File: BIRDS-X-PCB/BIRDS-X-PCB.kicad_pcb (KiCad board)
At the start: 2 copper layers, 85 x 85 mm, 0 parts

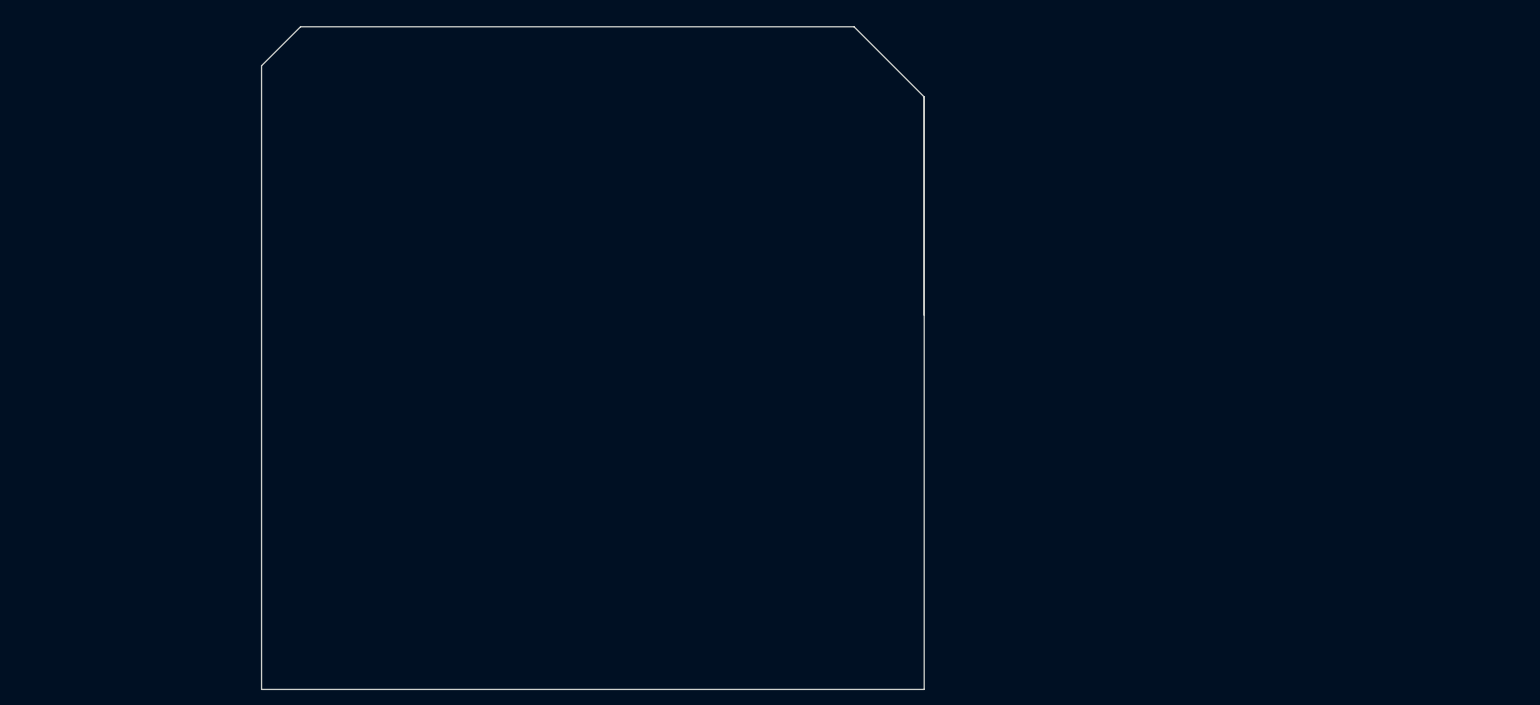
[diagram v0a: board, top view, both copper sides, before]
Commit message: Add core restricted layouts and lock them
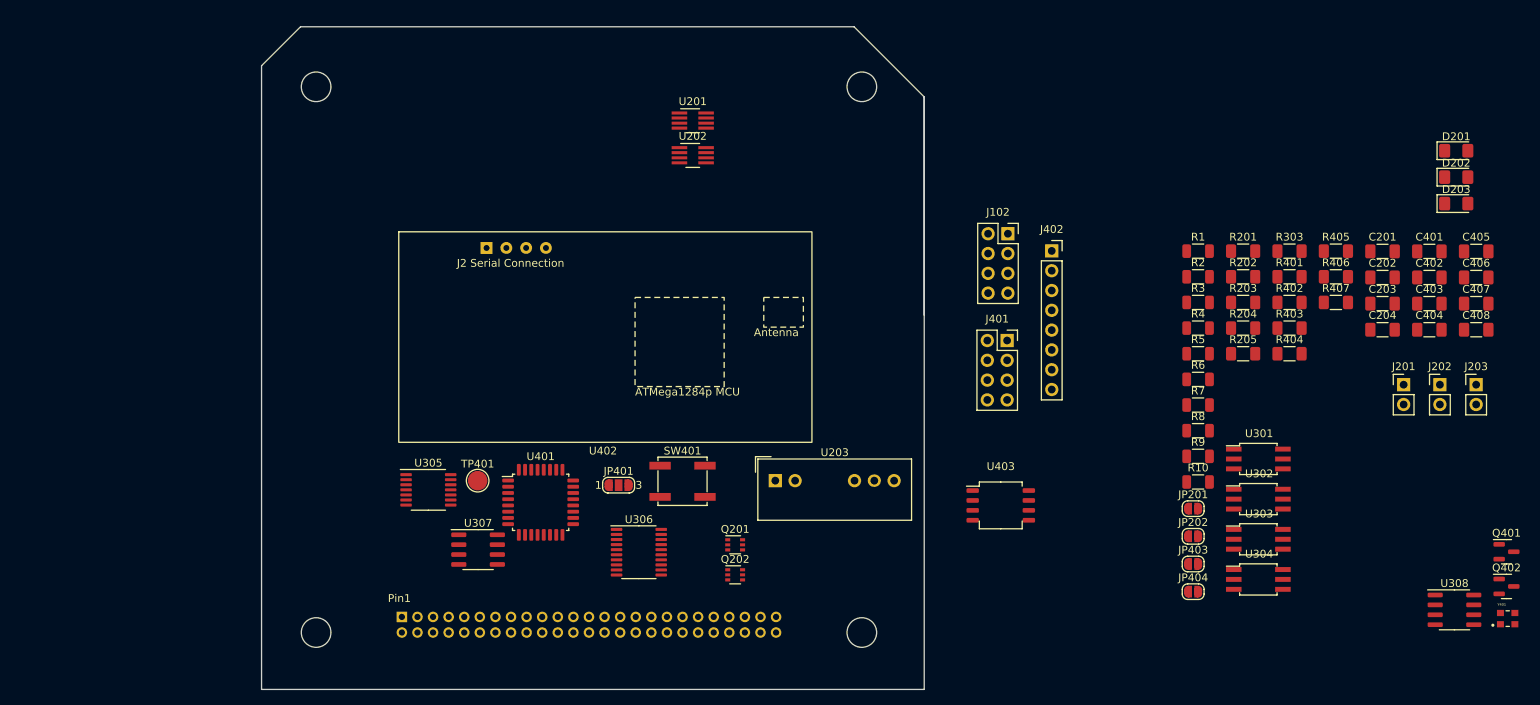
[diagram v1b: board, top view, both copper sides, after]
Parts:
- added C201: 10u, Capacitor_SMD:C_1206_3216Metric_Pad1.33x1.80mm_HandSolder, F.Cu at (225.3, 79.8)
- added C202: 10u, Capacitor_SMD:C_1206_3216Metric_Pad1.33x1.80mm_HandSolder, F.Cu at (225.3, 83.2)
- added C203: 4.7u, Capacitor_SMD:C_1206_3216Metric_Pad1.33x1.80mm_HandSolder, F.Cu at (225.3, 86.5)
- added C204: 10u, Capacitor_SMD:C_1206_3216Metric_Pad1.33x1.80mm_HandSolder, F.Cu at (225.3, 89.9)
- added C401: 100n, Capacitor_SMD:C_1206_3216Metric_Pad1.33x1.80mm_HandSolder, F.Cu at (231.3, 79.8)
- added C402: 100n, Capacitor_SMD:C_1206_3216Metric_Pad1.33x1.80mm_HandSolder, F.Cu at (231.3, 83.2)
- added C403: 4.7u, Capacitor_SMD:C_1206_3216Metric_Pad1.33x1.80mm_HandSolder, F.Cu at (231.3, 86.5)
- added C404: 10n, Capacitor_SMD:C_1206_3216Metric_Pad1.33x1.80mm_HandSolder, F.Cu at (231.3, 89.9)
- added C405: 100n, Capacitor_SMD:C_1206_3216Metric_Pad1.33x1.80mm_HandSolder, F.Cu at (237.3, 79.8)
- added C406: 4.7u, Capacitor_SMD:C_1206_3216Metric_Pad1.33x1.80mm_HandSolder, F.Cu at (237.3, 83.2)
- added C407: 100n, Capacitor_SMD:C_1206_3216Metric_Pad1.33x1.80mm_HandSolder, F.Cu at (237.3, 86.5)
- added C408: 4.7u, Capacitor_SMD:C_1206_3216Metric_Pad1.33x1.80mm_HandSolder, F.Cu at (237.3, 89.9)
- added D201: LED, LED_SMD:LED_1206_3216Metric_Pad1.42x1.75mm_HandSolder, F.Cu at (234.7, 66.9)
- added D202: LED, LED_SMD:LED_1206_3216Metric_Pad1.42x1.75mm_HandSolder, F.Cu at (234.7, 70.3)
- added D203: LED, LED_SMD:LED_1206_3216Metric_Pad1.42x1.75mm_HandSolder, F.Cu at (234.7, 73.7)
- added H101: MountingHole, BIRDS-X_Footprints_Lib:MountingHole_3.8mm, F.Cu at (88.5, 58.7)
- added H102: MountingHole, BIRDS-X_Footprints_Lib:MountingHole_3.8mm, F.Cu at (158.5, 58.7)
- added H103: MountingHole, BIRDS-X_Footprints_Lib:MountingHole_3.8mm, F.Cu at (88.5, 128.7)
- added H104: MountingHole, BIRDS-X_Footprints_Lib:MountingHole_3.8mm, F.Cu at (158.5, 128.7)
- added J101: LPC-50M2LG, Connector_PinHeader_2.00mm:PinHeader_2x25_P2.00mm_Horizontal, B.Cu at (99.5, 126.7)
- added J102: Conn_02x04_Odd_Even, Connector_PinSocket_2.54mm:PinSocket_2x04_P2.54mm_Vertical, F.Cu at (177.2, 77.5)
- added J201: Conn_01x02, Connector_PinHeader_2.54mm:PinHeader_1x02_P2.54mm_Vertical, F.Cu at (228.0, 96.9)
- added J202: Conn_01x02, Connector_PinHeader_2.54mm:PinHeader_1x02_P2.54mm_Vertical, F.Cu at (232.7, 96.9)
- added J203: Conn_01x02, Connector_PinHeader_2.54mm:PinHeader_1x02_P2.54mm_Vertical, F.Cu at (237.3, 96.9)
- added J401: Conn_02x04_Odd_Even, Connector_PinSocket_2.54mm:PinSocket_2x04_P2.54mm_Vertical, F.Cu at (177.1, 91.2)
- added J402: Conn_01x08, Connector_PinSocket_2.54mm:PinSocket_1x08_P2.54mm_Vertical, F.Cu at (182.9, 79.8)
- added JP201: Jumper_2_Open, Jumper:SolderJumper-2_P1.3mm_Open_RoundedPad1.0x1.5mm, F.Cu at (201.0, 112.8)
- added JP202: Jumper_2_Open, Jumper:SolderJumper-2_P1.3mm_Open_RoundedPad1.0x1.5mm, F.Cu at (201.0, 116.4)
- added JP401: Jumper_3_Open, Jumper:SolderJumper-3_P1.3mm_Open_RoundedPad1.0x1.5mm_NumberLabels, F.Cu at (127.3, 109.8)
- added JP403: Jumper_2_Open, Jumper:SolderJumper-2_P1.3mm_Open_RoundedPad1.0x1.5mm, F.Cu at (201.0, 119.9)
- added JP404: Jumper_2_Open, Jumper:SolderJumper-2_P1.3mm_Open_RoundedPad1.0x1.5mm, F.Cu at (201.0, 123.5)
- added Q201: SI1470DH, Package_TO_SOT_SMD:SOT-363_SC-70-6, F.Cu at (142.2, 117.5)
- added Q202: SI1470DH, Package_TO_SOT_SMD:SOT-363_SC-70-6, F.Cu at (142.2, 121.3)
- added Q401: BSS138, Package_TO_SOT_SMD:SOT-23, F.Cu at (241.2, 118.3)
- added Q402: BSS138, Package_TO_SOT_SMD:SOT-23, F.Cu at (241.2, 122.8)
- added R1: 390k, Resistor_SMD:R_1206_3216Metric, F.Cu at (201.6, 79.8)
- added R10: 3.6M, Resistor_SMD:R_1206_3216Metric, F.Cu at (201.6, 109.4)
- added R2: 10k, Resistor_SMD:R_1206_3216Metric, F.Cu at (201.6, 83.1)
- added R201: 0.025, PE1206FRE470R025L, Resistor_SMD:R_1206_3216Metric_Pad1.30x1.75mm_HandSolder, F.Cu at (207.4, 79.8)
- added R202: 0.025, PE1206FRE470R025L, Resistor_SMD:R_1206_3216Metric_Pad1.30x1.75mm_HandSolder, F.Cu at (207.4, 83.1)
- added R203: R, Resistor_SMD:R_1206_3216Metric_Pad1.30x1.75mm_HandSolder, F.Cu at (207.4, 86.4)
- added R204: R, Resistor_SMD:R_1206_3216Metric_Pad1.30x1.75mm_HandSolder, F.Cu at (207.4, 89.7)
- added R205: R, Resistor_SMD:R_1206_3216Metric_Pad1.30x1.75mm_HandSolder, F.Cu at (207.4, 92.9)
- added R3: 10M, Resistor_SMD:R_1206_3216Metric, F.Cu at (201.6, 86.4)
- added R303: 3.3k, Resistor_SMD:R_1206_3216Metric_Pad1.30x1.75mm_HandSolder, F.Cu at (213.4, 79.8)
- added R4: 3.6M, Resistor_SMD:R_1206_3216Metric, F.Cu at (201.6, 89.7)
- added R401: 3.3k, Resistor_SMD:R_1206_3216Metric_Pad1.30x1.75mm_HandSolder, F.Cu at (213.4, 83.1)
- added R402: 3.3k, Resistor_SMD:R_1206_3216Metric_Pad1.30x1.75mm_HandSolder, F.Cu at (213.4, 86.4)
- added R403: 10k, Resistor_SMD:R_1206_3216Metric_Pad1.30x1.75mm_HandSolder, F.Cu at (213.4, 89.7)
- added R404: 10k, Resistor_SMD:R_1206_3216Metric_Pad1.30x1.75mm_HandSolder, F.Cu at (213.4, 92.9)
- added R405: 10k, Resistor_SMD:R_1206_3216Metric_Pad1.30x1.75mm_HandSolder, F.Cu at (219.3, 79.8)
- added R406: 10k, Resistor_SMD:R_1206_3216Metric_Pad1.30x1.75mm_HandSolder, F.Cu at (219.3, 83.1)
- added R407: 10k, Resistor_SMD:R_1206_3216Metric_Pad1.30x1.75mm_HandSolder, F.Cu at (219.3, 86.4)
- added R5: 10M, Resistor_SMD:R_1206_3216Metric, F.Cu at (201.6, 92.9)
- added R6: 3.6M, Resistor_SMD:R_1206_3216Metric, F.Cu at (201.6, 96.2)
- added R7: 10M, Resistor_SMD:R_1206_3216Metric, F.Cu at (201.6, 99.5)
- added R8: 3.6M, Resistor_SMD:R_1206_3216Metric, F.Cu at (201.6, 102.8)
- added R9: 10M, Resistor_SMD:R_1206_3216Metric, F.Cu at (201.6, 106.1)
- added SW401: SW_Push, Button_Switch_SMD:SW_SPST_EVPBF, F.Cu at (135.5, 109.3)
- added TP401: TestPoint, TestPoint:TestPoint_Pad_D2.5mm, F.Cu at (109.2, 109.2)
- added U201: LTC4361-X, Package_TO_SOT_SMD:TSOT-23-8_HandSoldering, F.Cu at (136.8, 63.0)
- added U202: LTC4361-X, Package_TO_SOT_SMD:TSOT-23-8_HandSoldering, F.Cu at (136.8, 67.5)
- added U203: 0.1S7B_3UP, BIRDS-X_Footprints_Lib:Converter_DCDC_Gaptec_0.1S7B_3UP_THT, F.Cu at (147.4, 109.2)
- added U301: VT01, Package_SO:SO-6_4.4x3.6mm_P1.27mm, F.Cu at (209.4, 106.4)
- added U302: VT01, Package_SO:SO-6_4.4x3.6mm_P1.27mm, F.Cu at (209.4, 111.6)
- added U303: VT01, Package_SO:SO-6_4.4x3.6mm_P1.27mm, F.Cu at (209.4, 116.7)
- added U304: VT01, Package_SO:SO-6_4.4x3.6mm_P1.27mm, F.Cu at (209.4, 121.9)
- added U305: TL974IPWR, Package_SO:TSSOP-14_4.4x5mm_P0.65mm, F.Cu at (102.9, 110.4)
- added U306: ADG734, Package_SO:TSSOP-20_4.4x6.5mm_P0.65mm, F.Cu at (129.9, 118.4)
- added U307: LM335DT, Package_SO:SOIC-8_3.9x4.9mm_P1.27mm, F.Cu at (109.3, 118.1)
- added U308: LM334M, Package_SO:SOIC-8_3.9x4.9mm_P1.27mm, F.Cu at (234.5, 125.8)
- added U401: STM32G031K8Tx, Package_QFP:LQFP-32_7x7mm_P0.8mm, F.Cu at (117.3, 112.0)
- added U402: MTT4B-Mini, BIRDS-X_Footprints_Lib:MTT4B-Mini, F.Cu at (125.6, 90.8)
- added U403: MT29F2G01ABAGDWB-IT-G_TR, BIRDS-X_Footprints_Lib:U-PDFN-8_6x8mm_P1.27mm, F.Cu at (176.3, 112.4)
- added Y401: ECS-2520SMV-080-FN-TR, lib:OSC_ECS-2520SMV-080-FN-TR, F.Cu at (241.3, 126.9)
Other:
- board text added: "(0,0) is (81,51)"
- board text added: "Pin1"

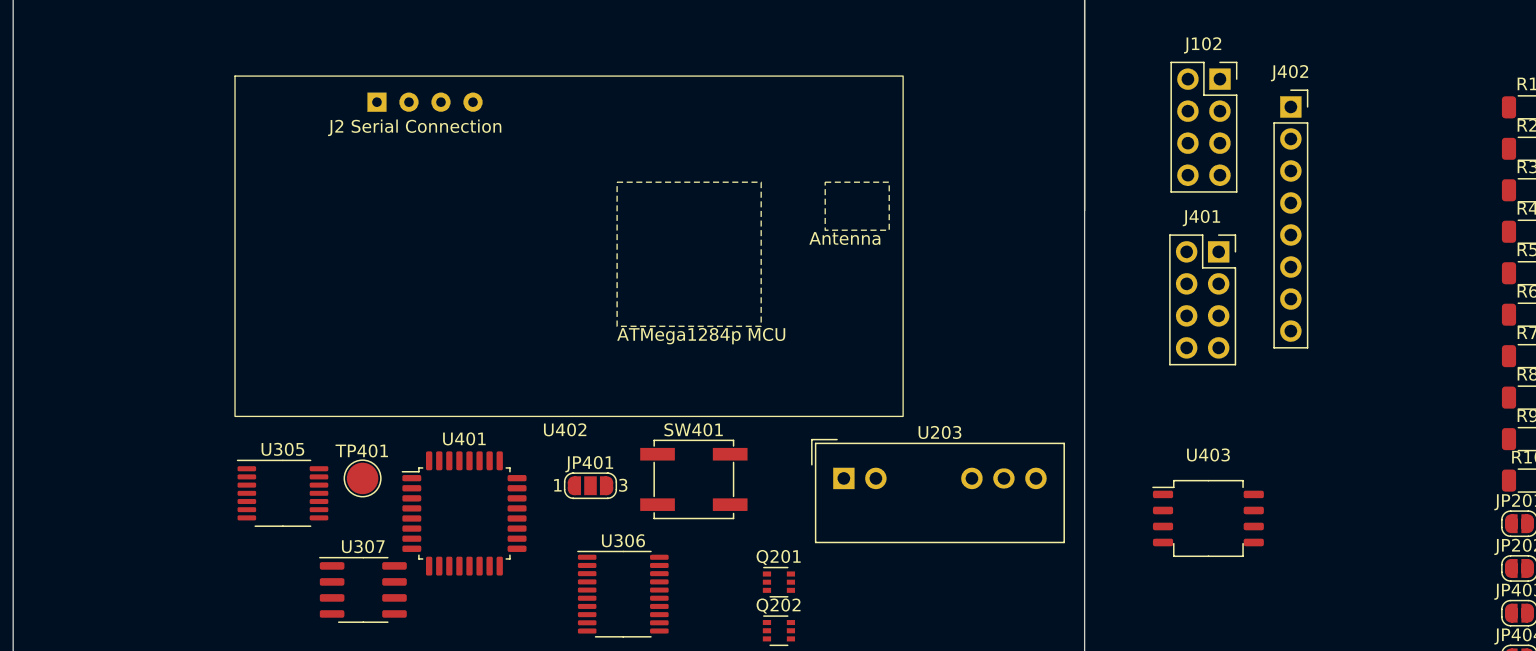
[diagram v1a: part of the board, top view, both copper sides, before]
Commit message: Fix flash signals, fix footprints
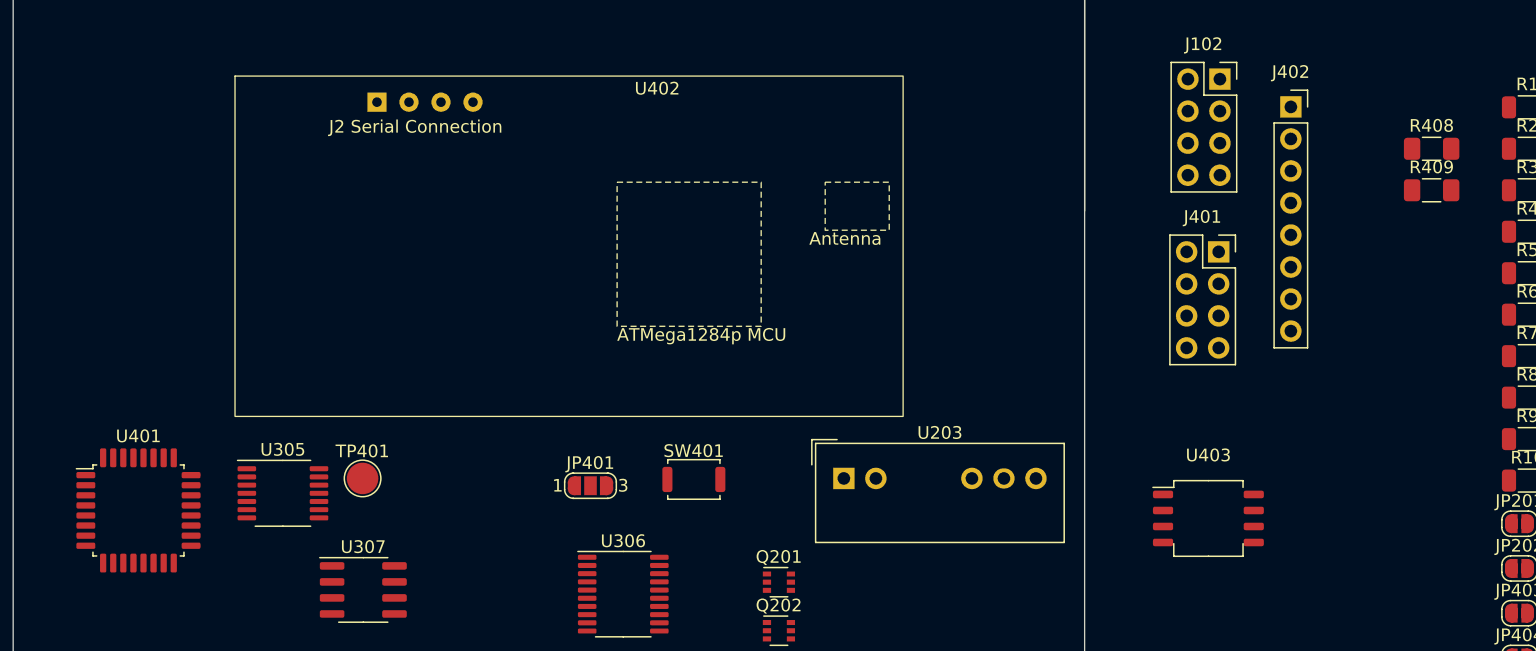
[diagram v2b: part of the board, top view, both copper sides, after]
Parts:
- added R408: 10k, Resistor_SMD:R_1206_3216Metric_Pad1.30x1.75mm_HandSolder, F.Cu at (194.0, 83.1)
- added R409: 10k, Resistor_SMD:R_1206_3216Metric_Pad1.30x1.75mm_HandSolder, F.Cu at (194.0, 86.4)
- SW401: footprint Button_Switch_SMD:SW_SPST_EVPBF -> Button_Switch_SMD:SW_Push_SPST_NO_Alps_SKRK
- moved U401 25.9 mm to (91.4, 111.8)

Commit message: Add notes from schematic review session
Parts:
- moved Q401 56.7 mm to (184.5, 121.5)
- moved Q402 56.7 mm to (184.5, 125.9)
- moved U308 56.7 mm to (177.9, 128.9)
- moved Y401 56.7 mm to (184.7, 130.0)
- moved U203 46.9 mm to (111.8, 78.7)
- moved U401 40.0 mm to (126.1, 91.8)
- moved U402 25.5 mm to (151.1, 91.4), turned to -90 degrees
- moved Q201 21.9 mm to (120.3, 117.5)
- moved SW401 4.67 mm to (131.6, 106.7)
- moved JP401 4.14 mm to (123.2, 109.8)
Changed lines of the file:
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@@
   )
   (footprint "Button_Switch_SMD:SW_Push_SPST_NO_Alps_SKRK" (layer "F.Cu")
-    (at 135.5 109.3)
+    (at 131.64 106.68)
     (descr "http://www.alps.com/prod/info/E/HTML/Tact/SurfaceMount/SKRK/SKRKAHE020.html")
     (tags "SMD SMT button")
@@
   )
   (footprint "lib:OSC_ECS-2520SMV-080-FN-TR" (layer "F.Cu")
-    (at 241.345 126.915)
+    (at 184.69 130.03)
     (property "Sheetfile" "MicrocontrollerSheet.kicad_sch")
     (property "Sheetname" "MicrocontrollerSheet")
@@
   )
   (footprint "BIRDS-X_Footprints_Lib:MTT4B-Mini" (layer "F.Cu")
-    (at 125.6 90.8)
+    (at 151.13 91.44 -90)
     (property "Sheetfile" "MicrocontrollerSheet.kicad_sch")
     (property "Sheetname" "MicrocontrollerSheet")
     (attr through_hole)
-    (fp_text reference "U402" (at 7 -12.5 unlocked) (layer "F.SilkS")
+    (fp_text reference "U402" (at 7 -12.5 -90 unlocked) (layer "F.SilkS")
         (effects (font (size 1 1) (thickness 0.1)))
     )
-    (fp_text value "MTT4B-Mini" (at 7 -11 unlocked) (layer "F.Fab")
+    (fp_text value "MTT4B-Mini" (at 7 -11 -90 unlocked) (layer "F.Fab")
         (effects (font (size 1 1) (thickness 0.15)))
     )
-    (fp_text user "Antenna" (at 19.05 0 unlocked) (layer "F.SilkS")
+    (fp_text user "Antenna" (at 19.05 0 -90 unlocked) (layer "F.SilkS")
         (effects (font (size 1 1) (thickness 0.1)) (justify left bottom))
     )
-    (fp_text user "J2 Serial Connection" (at -19.05 -8.89 unlocked) (layer "F.SilkS")
+    (fp_text user "J2 Serial Connection" (at -19.05 -8.89 -90 unlocked) (layer "F.SilkS")
         (effects (font (size 1 1) (thickness 0.1)) (justify left bottom))
     )
-    (fp_text user "ATMega1284p MCU" (at 3.81 7.62 unlocked) (layer "F.SilkS")
+    (fp_text user "ATMega1284p MCU" (at 3.81 7.62 -90 unlocked) (layer "F.SilkS")
         (effects (font (size 1 1) (thickness 0.1)) (justify left bottom))
     )
-    (fp_text user "${REFERENCE}" (at 7 -9.5 unlocked) (layer "F.Fab")
+    (fp_text user "${REFERENCE}" (at 7 -9.5 -90 unlocked) (layer "F.Fab")
         (effects (font (size 1 1) (thickness 0.15)))
     )
@@
     (fp_rect (start -26.5 -13.5) (end 26.5 13.5)
       (stroke (width 0.05) (type default)) (fill none) (layer "F.CrtYd"))
-    (pad "J2-1" thru_hole rect (at -15.24 -11.43) (size 1.524 1.524) (drill 0.762) (layers "*.Cu" "*.Mask")
+    (pad "J2-1" thru_hole rect (at -15.24 -11.43 270) (size 1.524 1.524) (drill 0.762) (layers "*.Cu" "*.Mask")
       (net 2 "GND") (pinfunction "GND") (pintype "input"))
-    (pad "J2-2" thru_hole circle (at -12.7 -11.43) (size 1.524 1.524) (drill 0.762) (layers "*.Cu" "*.Mask")
+    (pad "J2-2" thru_hole circle (at -12.7 -11.43 270) (size 1.524 1.524) (drill 0.762) (layers "*.Cu" "*.Mask")
       (net 60 "Net-(J401-Pin_3)") (pinfunction "PD0_UART_RX_EXT_TO_MTT4B") (pintype "input"))
-    (pad "J2-3" thru_hole circle (at -10.16 -11.43) (size 1.524 1.524) (drill 0.762) (layers "*.Cu" "*.Mask")
+    (pad "J2-3" thru_hole circle (at -10.16 -11.43 270) (size 1.524 1.524) (drill 0.762) (layers "*.Cu" "*.Mask")
       (net 1 "+5V") (pinfunction "VCC") (pintype "input"))
-    (pad "J2-4" thru_hole circle (at -7.62 -11.43) (size 1.524 1.524) (drill 0.762) (layers "*.Cu" "*.Mask")
+    (pad "J2-4" thru_hole circle (at -7.62 -11.43 270) (size 1.524 1.524) (drill 0.762) (layers "*.Cu" "*.Mask")
       (net 61 "Net-(J401-Pin_7)") (pinfunction "PD1_UART_TX_MTT4B_TO_EXT") (pintype "input"))
   )
@@
   )
   (footprint "Package_SO:SOIC-8_3.9x4.9mm_P1.27mm" (layer "F.Cu")
-    (at 234.52 125.79)
+    (at 177.865 128.905)
     (descr "SOIC, 8 Pin (JEDEC MS-012AA, https://www.analog.com/media/en/package-pcb-resources/package/pkg_pdf/soic_narrow-r/r_8.pdf), generated with kicad-footprint-generator ipc_gullwing_generator.py")
     (tags "SOIC SO")
@@
   )
   (footprint "Package_QFP:LQFP-32_7x7mm_P0.8mm" (layer "F.Cu")
-    (at 91.44 111.76)
+    (at 126.095 91.84)
     (descr "LQFP, 32 Pin (https://www.nxp.com/docs/en/package-information/SOT358-1.pdf), generated with kicad-footprint-generator ipc_gullwing_generator.py")
     (tags "LQFP QFP")
@@
   )
   (footprint "Package_TO_SOT_SMD:SOT-23" (layer "F.Cu")
-    (at 241.19 118.34)
+    (at 184.535 121.455)
     (descr "SOT, 3 Pin (https://www.jedec.org/system/files/docs/to-236h.pdf variant AB), generated with kicad-footprint-generator ipc_gullwing_generator.py")
     (tags "SOT TO_SOT_SMD")
@@
   )
   (footprint "BIRDS-X_Footprints_Lib:Converter_DCDC_Gaptec_0.1S7B_3UP_THT" (layer "F.Cu")
-    (at 147.4 109.22)
+    (at 111.76 78.74)
     (descr "Murata MGJ2DxxxxxxSC, 19.5x9.8x12.5mm, 5.2kVDC Isolated, 2W, SIP package style, https://power.murata.com/data/power/ncl/kdc_mgj2.pdf")
     (tags "Murata MGJ2DxxxxxxSC")
@@
   )
   (footprint "Package_TO_SOT_SMD:SOT-23" (layer "F.Cu")
-    (at 241.19 122.79)
+    (at 184.535 125.905)
     (descr "SOT, 3 Pin (https://www.jedec.org/system/files/docs/to-236h.pdf variant AB), generated with kicad-footprint-generator ipc_gullwing_generator.py")
     (tags "SOT TO_SOT_SMD")
@@
   )
   (footprint "Jumper:SolderJumper-3_P1.3mm_Open_RoundedPad1.0x1.5mm_NumberLabels" (layer "F.Cu")
-    (at 127.3 109.8)
+    (at 123.16 109.8)
     (descr "SMD Solder 3-pad Jumper, 1x1.5mm rounded Pads, 0.3mm gap, open, labeled with numbers")
     (tags "solder jumper open")
@@
   )
   (footprint "Package_TO_SOT_SMD:SOT-363_SC-70-6" (layer "F.Cu")
-    (at 142.25 117.45)
+    (at 120.33 117.45)
     (descr "SOT-363, SC-70-6")
     (tags "SOT-363 SC-70-6")
